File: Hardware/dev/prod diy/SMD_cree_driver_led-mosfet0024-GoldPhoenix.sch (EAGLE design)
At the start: 15 parts, among them Q1 BSS123, Q2 BSS123, Q3 BSS123, Q4 BSS123, Q5 NSI50350AST3G, Q6 NSI50350AST3G, Q7 NSI50350AST3G, Q8 NSI50350AST3G

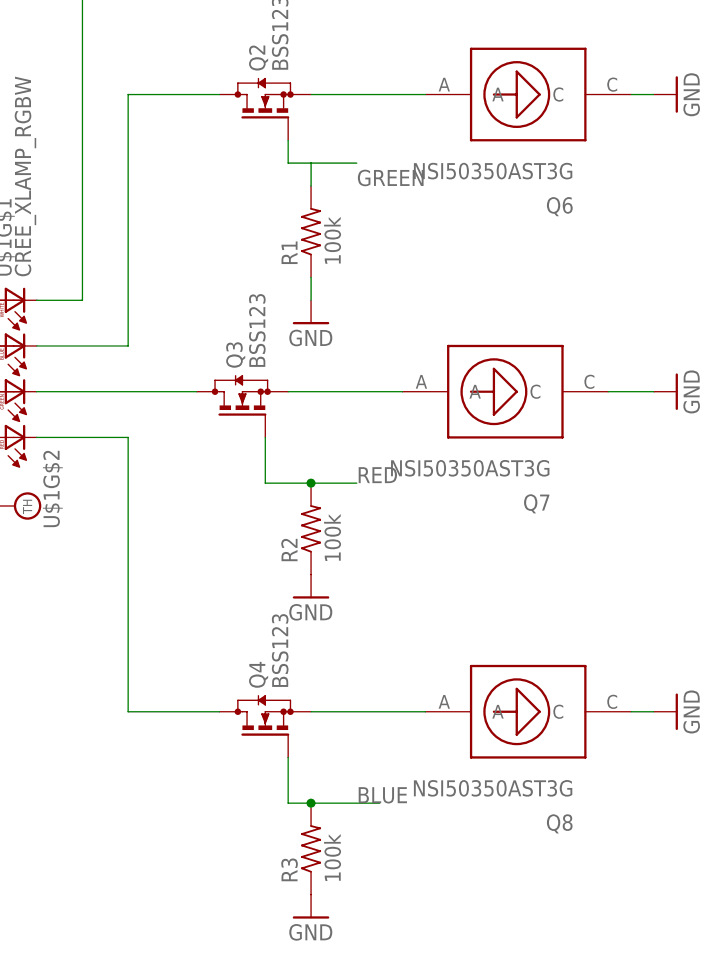
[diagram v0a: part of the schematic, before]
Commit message: fixed silk error on LED board
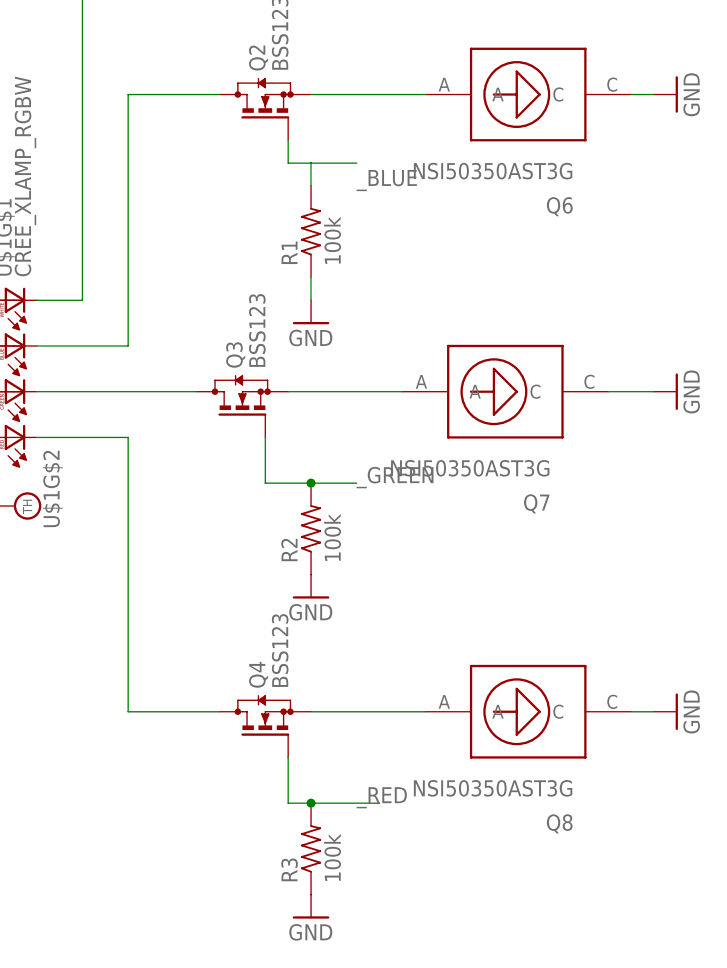
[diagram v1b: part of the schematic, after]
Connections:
- net BLUE renamed _RED
- net BLUE_OUT renamed GREEN_PWM_IN
- net GREEN renamed _BLUE
- net GREEN_OUT renamed RED_PWM_IN
- net N$1 renamed BLUE_DRIVER
- net N$13 renamed WHITE_DRIVER
- net N$2 renamed GREEN_DRIVER
- net N$3 renamed RED_DRIVER
- net N$5 renamed WHITE_PWM_IN
- net RED renamed _GREEN
- net RED_OUT renamed BLUE_PWM_IN
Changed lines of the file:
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@@
 </segment>
 </net>
-<net name="BLUE" class="1">
+<net name="_RED" class="1">
 <segment>
 <label x="55.88" y="-10.16" size="1.778" layer="95"/>
@@
 </segment>
 </net>
-<net name="RED" class="1">
+<net name="_GREEN" class="1">
 <segment>
 <label x="55.88" y="25.4" size="1.778" layer="95"/>
@@
 </segment>
 </net>
-<net name="GREEN" class="1">
+<net name="_BLUE" class="1">
 <segment>
 <label x="55.88" y="58.42" size="1.778" layer="95"/>
@@
 </segment>
 </net>
-<net name="N$3" class="0">
+<net name="RED_DRIVER" class="0">
 <segment>
 <wire x1="30.48" y1="30.48" x2="20.32" y2="30.48" width="0.1524" layer="91"/>
@@
 </segment>
 </net>
-<net name="N$1" class="0">
+<net name="BLUE_DRIVER" class="0">
 <segment>
 <wire x1="30.48" y1="40.64" x2="20.32" y2="40.64" width="0.1524" layer="91"/>
@@
 </segment>
 </net>
-<net name="N$2" class="0">
+<net name="GREEN_DRIVER" class="0">
 <segment>
 <wire x1="20.32" y1="35.56" x2="38.1" y2="35.56" width="0.1524" layer="91"/>
@@
 </segment>
 </net>
-<net name="GREEN_OUT" class="1">
+<net name="RED_PWM_IN" class="1">
 <segment>
 <wire x1="-33.02" y1="48.26" x2="-27.94" y2="48.26" width="0.1524" layer="91"/>
@@
 </segment>
 </net>
-<net name="RED_OUT" class="1">
+<net name="BLUE_PWM_IN" class="1">
 <segment>
 <wire x1="-33.02" y1="43.18" x2="-27.94" y2="43.18" width="0.1524" layer="91"/>
@@
 </segment>
 </net>
-<net name="BLUE_OUT" class="1">
+<net name="GREEN_PWM_IN" class="1">
 <segment>
 <wire x1="-33.02" y1="38.1" x2="-27.94" y2="38.1" width="0.1524" layer="91"/>
@@
 </segment>
 </net>
-<net name="N$5" class="0">
+<net name="WHITE_PWM_IN" class="0">
 <segment>
 <pinref part="PL1" gate="-1" pin="S"/>
@@
 </segment>
 </net>
-<net name="N$13" class="0">
+<net name="WHITE_DRIVER" class="0">
 <segment>
 <wire x1="25.4" y1="109.22" x2="40.64" y2="109.22" width="0.1524" layer="91"/>
